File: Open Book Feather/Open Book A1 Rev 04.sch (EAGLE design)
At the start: 125 parts, among them J1 SJ-43514-SMT, J2 10118193-0001LF, Q1 DMG341, Q2 IRLML0100, SW1 SPDT_SWITCH, U1 AP2112-3.3, U2 MCP73831T-2ACI/OT, U3 ATSAMD51J64-TQFP(10X10), U4 GD25Q16C (or GD25Q32C), U5 74AC165D, U6 GD25Q16C (or GD25Q32C), U8 MAX4466EXK+T, X1 JSTPH, X2 2x5 0.05" SWD

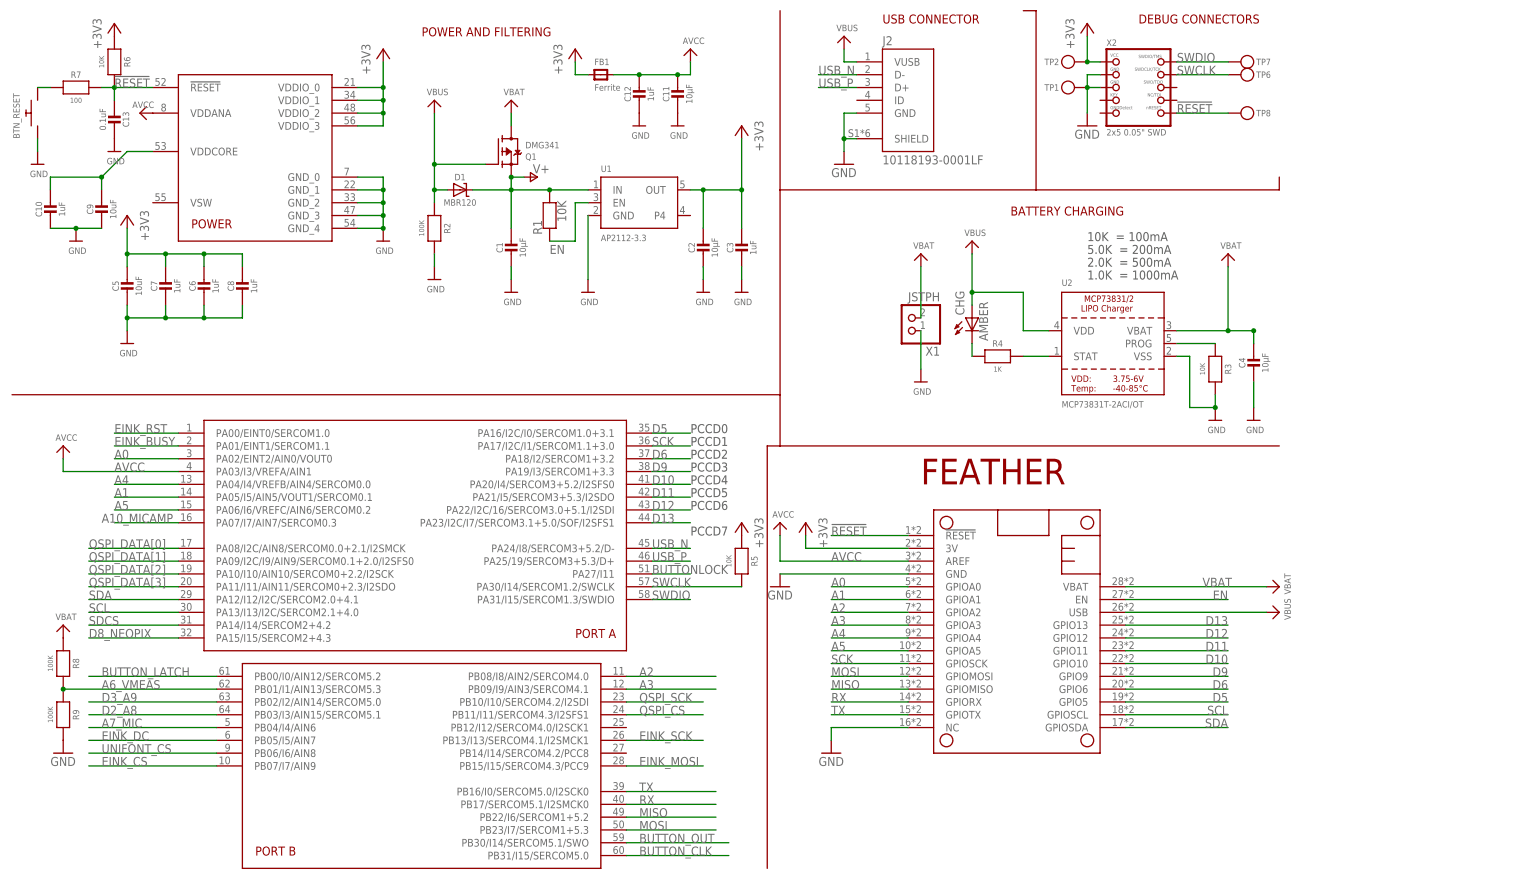
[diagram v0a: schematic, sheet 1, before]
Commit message: resistor array to monitor both VBAT and VBUS
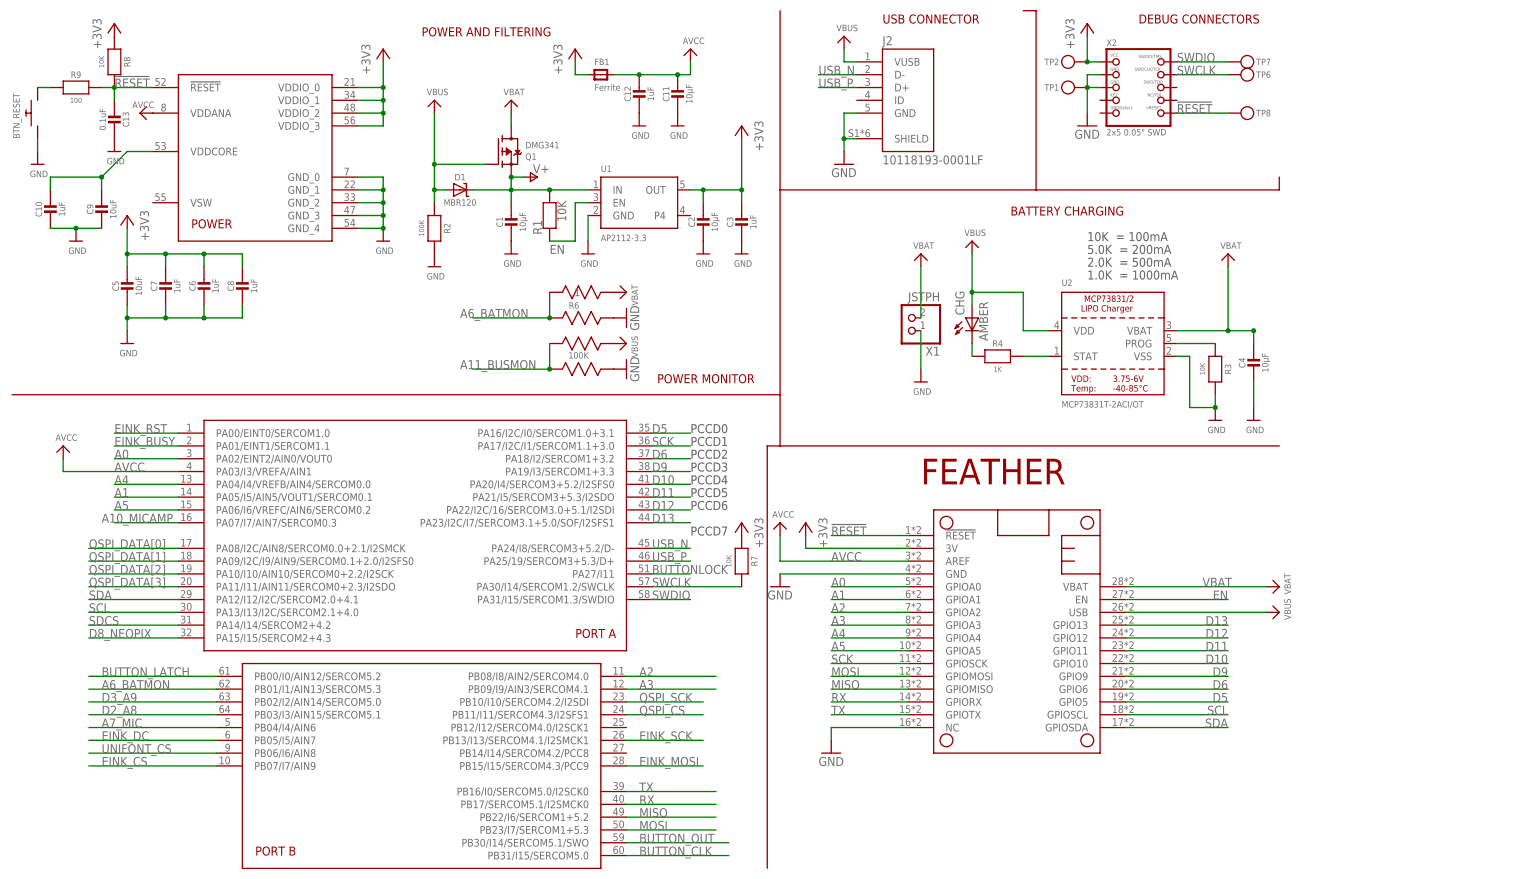
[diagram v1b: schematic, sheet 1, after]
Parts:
- removed R5: 10K, microbuilder:RESISTOR0805_10MGAP
- R6: value 10K -> 100K; device microbuilder:RESISTOR0805_10MGAP -> resistor array:EXB-V8V103JV
- R7: value 100 -> 10K
- R8: value 100K -> 10K; device microbuilder:RESISTOR0805_NOOUTLINE -> microbuilder:RESISTOR0805_10MGAP
- R9: value 100K -> 100; device microbuilder:RESISTOR0805_NOOUTLINE -> microbuilder:RESISTOR0805_10MGAP
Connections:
- removed net A6_VMEAS: R8.2, R9.1, U3G$2.PB01/I1/AIN13/SERCOM5.3
- new net A11_BUSMON: R6.3, R6.4
- new net A6_BATMON: R6.1, R6.2, U3G$2.PB01/I1/AIN13/SERCOM5.3
- net !RESET: now also R8.2, R9.2; no longer R6.2, R7.2
- net +3V3: now also R7.1, R8.1; no longer R5.1, R6.1
- net GND: now also R6.5, R6.7; no longer R9.2
- net N$1: now also R9.1; no longer R7.1
- net SWCLK: now also R7.2; no longer R5.2
- net VBAT: now also R6.8; no longer R8.1
- net VBUS: now also R6.6
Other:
- note added: "POWER MONITOR"
- moved on the sheet: C1, C2, C3, R7, R8, R9

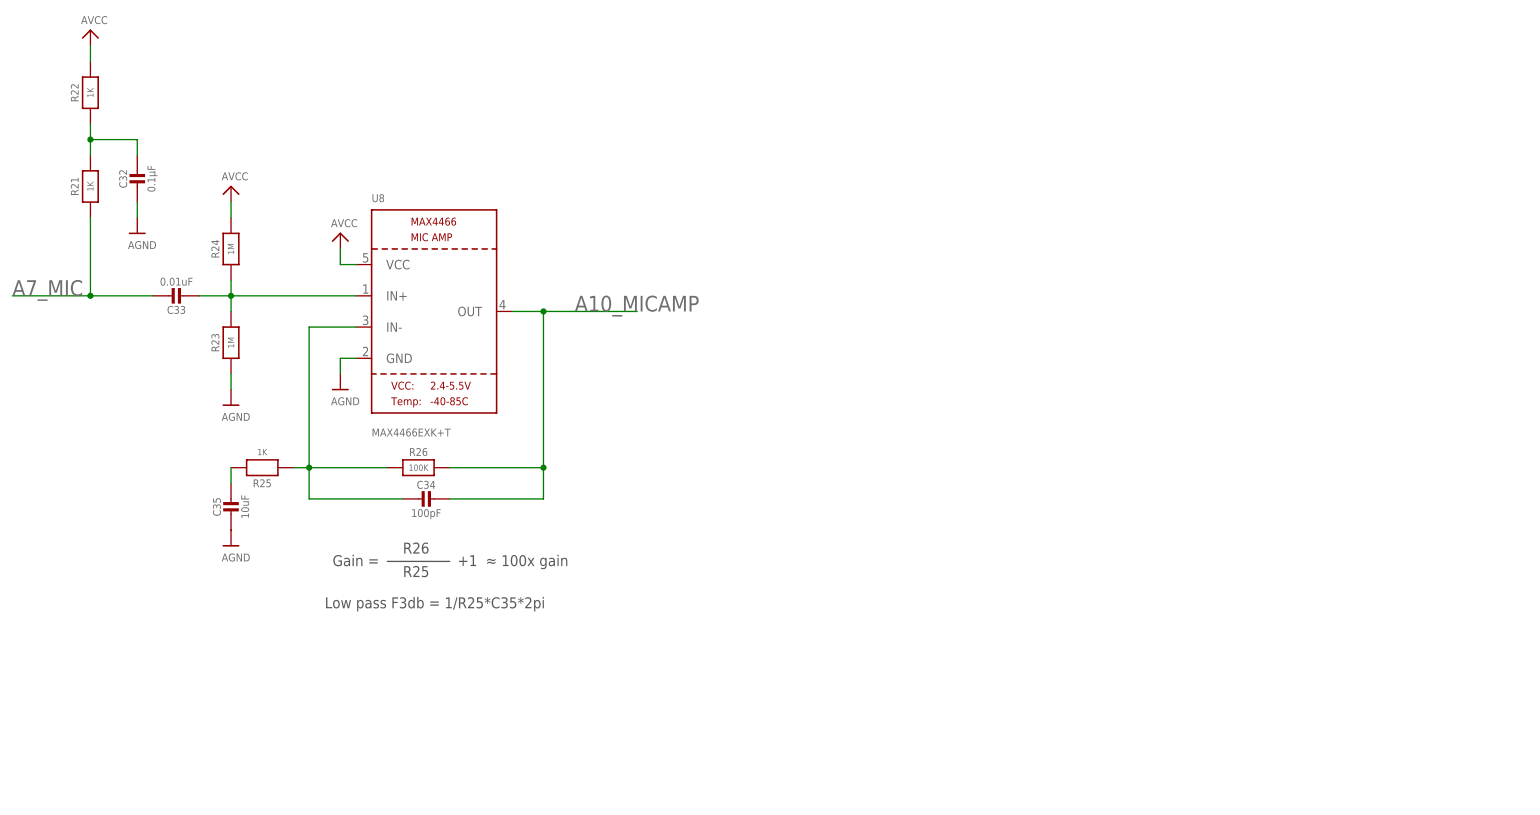
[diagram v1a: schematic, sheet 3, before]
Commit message: use max4468 for mic amp shutdown capability
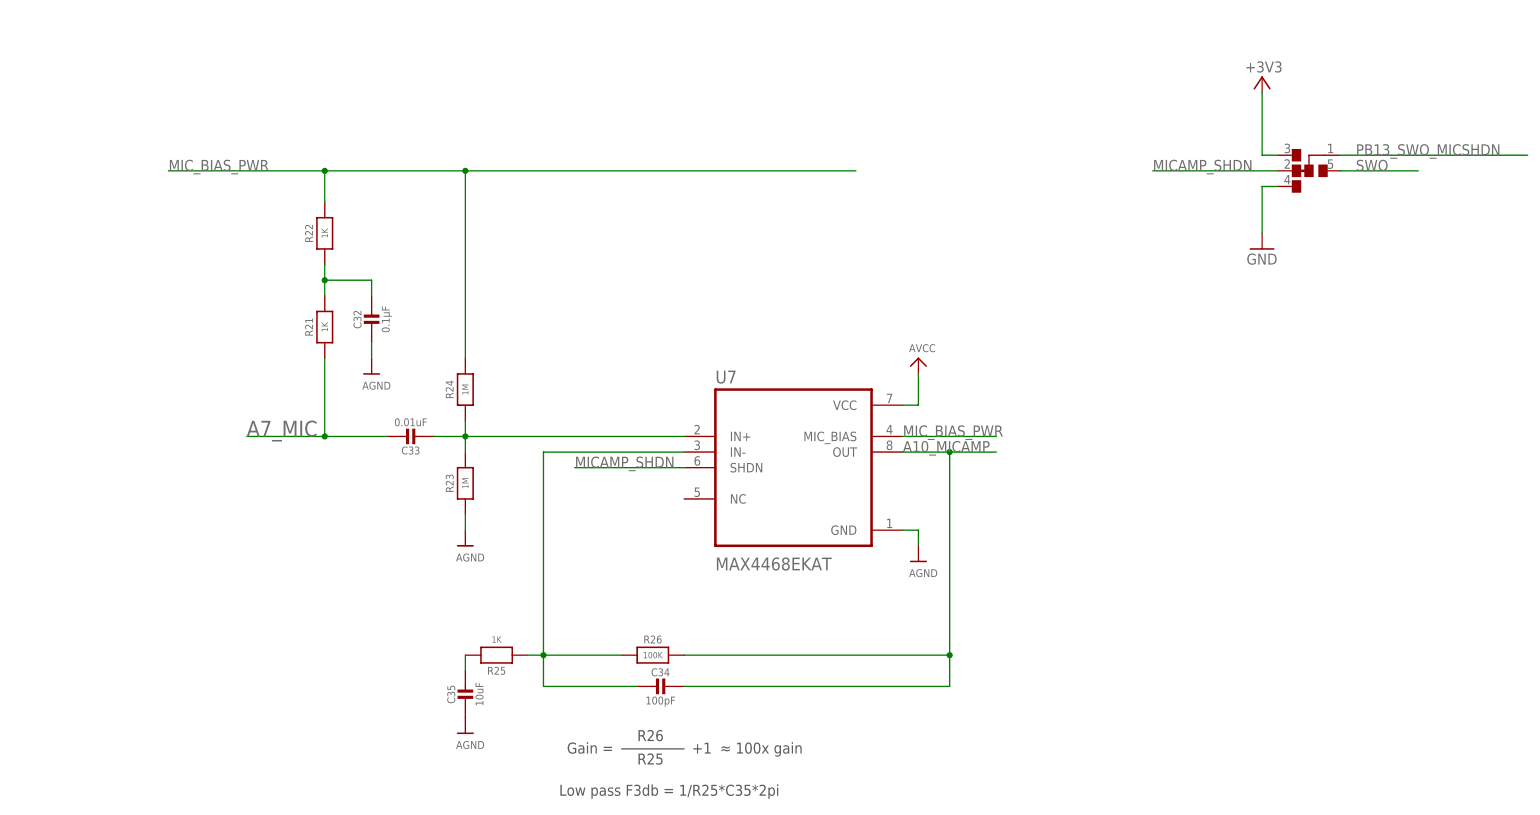
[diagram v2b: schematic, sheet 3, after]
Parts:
- removed U8: MAX4466EXK+T, microbuilder:AUDIOAMP_MAX4466
- added SJ1: SOLDERJUMPER_FIVEWAY, My Stuff:SOLDERJUMPER_FIVEWAY
- added U7: MAX4468EKAT, MAX4468EKAT:MAX4468EKAT
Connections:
- removed net N$67: C33.2, R23.2, R24.1, U8.IN+
- new net MICAMP_SHDN: SJ1.2, U7.SHDN
- new net MIC_BIAS_PWR: R22.2, R24.2, U7.MIC_BIAS
- new net N$6: C34.2, R25.1, R26.1, U7.IN-
- new net PB13_SWO_MICSHDN: SJ1.1, U3G$2.PB31/I15/SERCOM5.0
- new net SWO: SJ1.5, X2.SWO
- net +3V3: now also SJ1.3
- net A10_MICAMP: now also U7.OUT; no longer U8.OUT
- net AGND: now also U7.GND; no longer U8.GND
- net AVCC: now also U7.VCC; no longer R22.2, R24.2, U8.VCC
- net BUTTON_CLK: now also U3G$2.PB14/I14/SERCOM4.2/PCC8; no longer U3G$2.PB31/I15/SERCOM5.0
- net BUTTON_LATCH: now also U3G$2.PB12/I12/SERCOM4.0/I2SCK1; no longer U3G$2.PB00/I0/AIN12/SERCOM5.2
- net GND: now also SJ1.4
- net N$68: now also C33.2, R23.2, R24.1, U7.IN+; no longer C34.2, R25.1, R26.1, U8.IN-
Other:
- note added: "The MAX4468 has a shutdown pin. When MICAMP_SHDN goes high, the device turns off, AND it switches off MIC_BIAS_PWR, which saves us some fractional milliamps."
- moved on the sheet: C32, C33, C34, C35, R21, R22, R23, R24, R25, R26

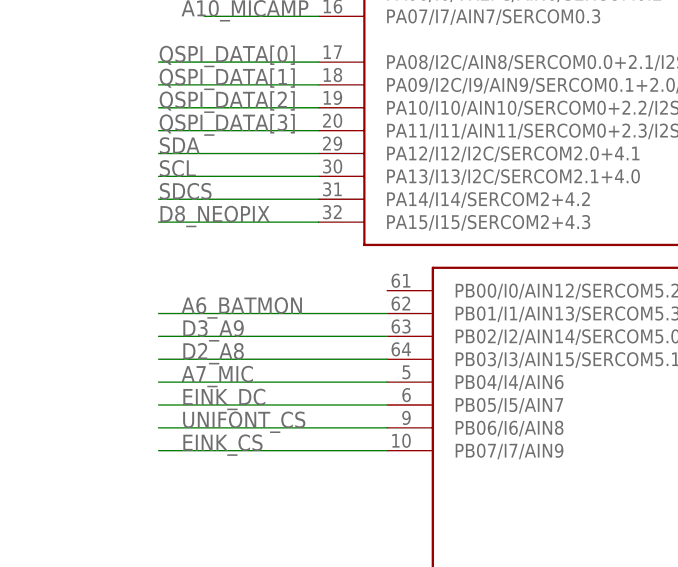
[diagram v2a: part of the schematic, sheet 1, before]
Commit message: route A11/VBUSMON
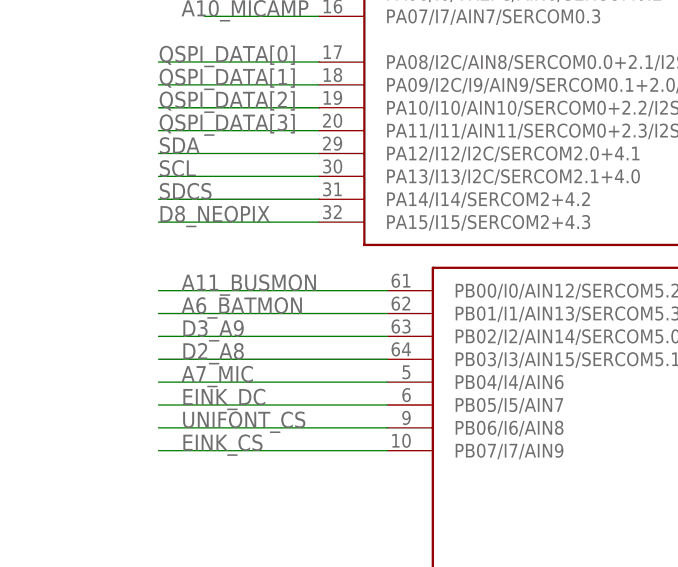
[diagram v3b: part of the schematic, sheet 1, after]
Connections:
- net A11_BUSMON: now also U3G$2.PB00/I0/AIN12/SERCOM5.2
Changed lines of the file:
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@@
 <junction x="416.56" y="109.22"/>
+</segment>
+<segment>
+<pinref part="U3" gate="G$2" pin="PB00/I0/AIN12/SERCOM5.2"/>
+<wire x1="350.52" y1="48.26" x2="325.12" y2="48.26" width="0.1524" layer="91"/>
+<label x="327.66" y="48.26" size="1.778" layer="95"/>
 </segment>
 </net>

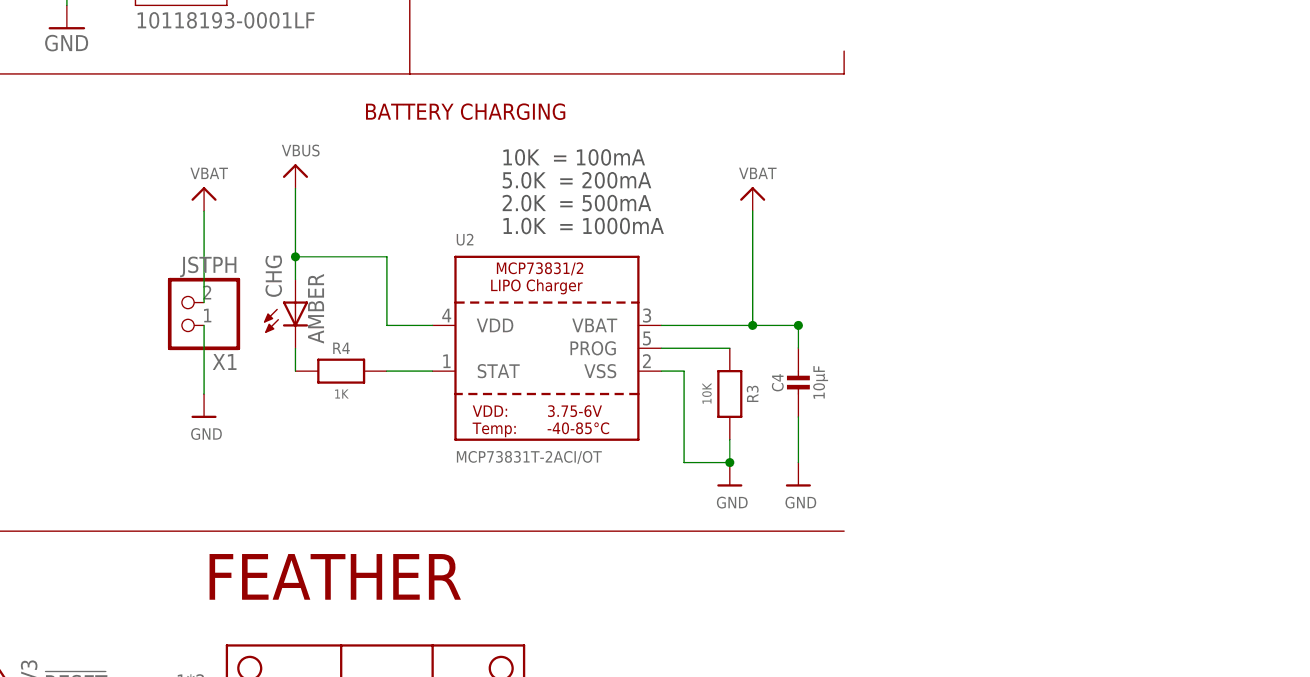
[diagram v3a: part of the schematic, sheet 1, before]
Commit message: add green led for full battery
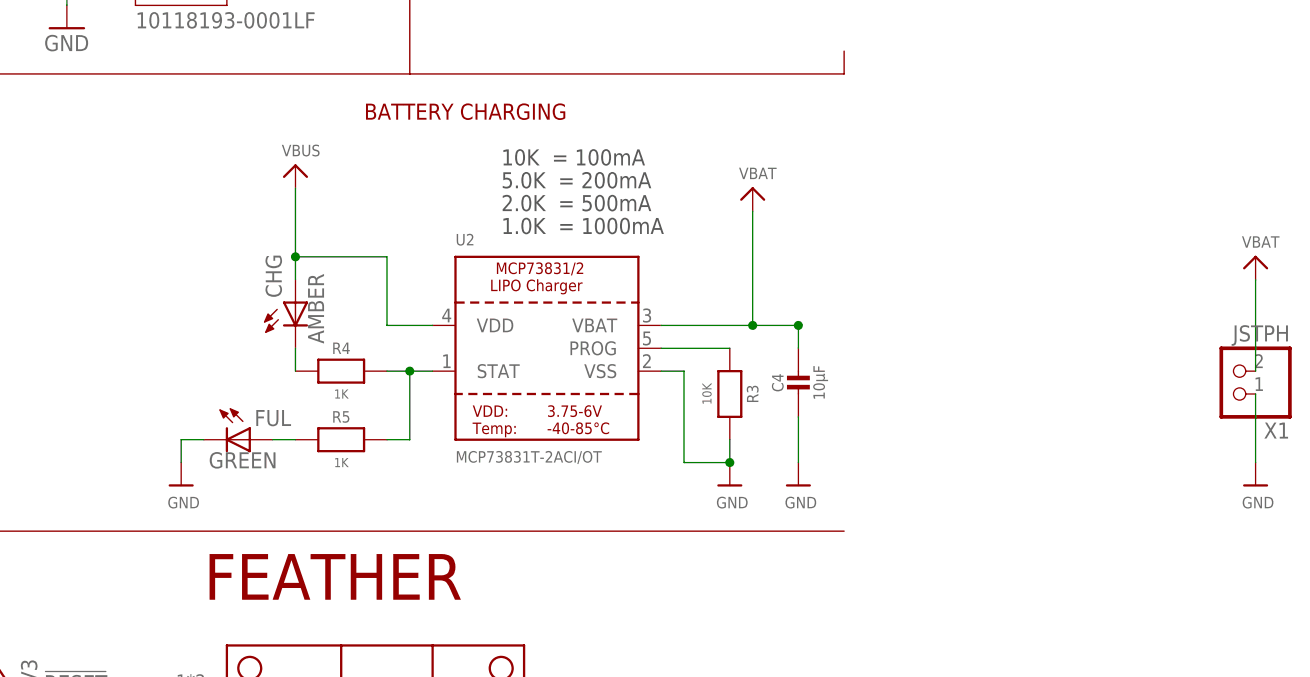
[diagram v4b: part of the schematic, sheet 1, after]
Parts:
- added FUL: GREEN, adafruit:LEDCHIP-LED0805
- added R5: 1K, microbuilder:RESISTOR0805_NOOUTLINE
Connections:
- removed net N$5: R4.2, U2.STAT
- new net N$9: FUL.A, R5.1
- new net STAT: R4.2, R5.2, U2.STAT
- net GND: now also FUL.C
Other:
- moved on the sheet: X1

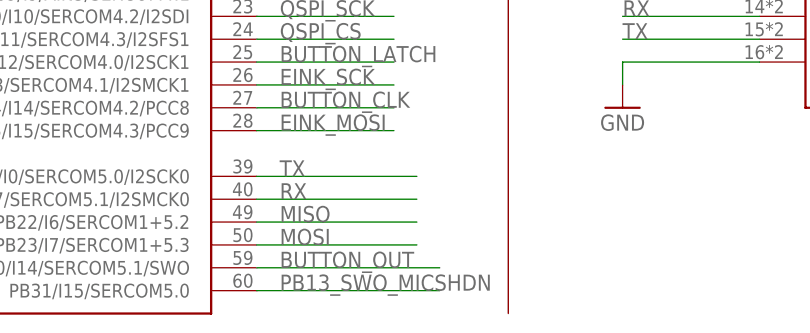
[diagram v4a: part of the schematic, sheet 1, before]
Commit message: fix typo in net name
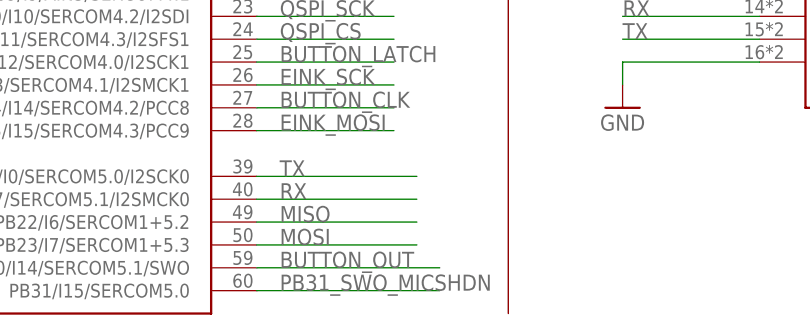
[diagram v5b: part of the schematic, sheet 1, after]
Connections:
- net PB13_SWO_MICSHDN renamed PB31_SWO_MICSHDN
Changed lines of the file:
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@@
 </segment>
 </net>
-<net name="PB13_SWO_MICSHDN" class="0">
+<net name="PB31_SWO_MICSHDN" class="0">
 <segment>
 <pinref part="U3" gate="G$2" pin="PB31/I15/SERCOM5.0"/>
@@
 </segment>
 </net>
-<net name="PB13_SWO_MICSHDN" class="0">
+<net name="PB31_SWO_MICSHDN" class="0">
 <segment>
 <pinref part="SJ1" gate="G$1" pin="1"/>
